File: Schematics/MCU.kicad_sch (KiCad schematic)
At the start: 28 parts, among them J1 Microsemi_FlashPro-JTAG-10, U1 STM32F405RGT6, Y1 8mhz

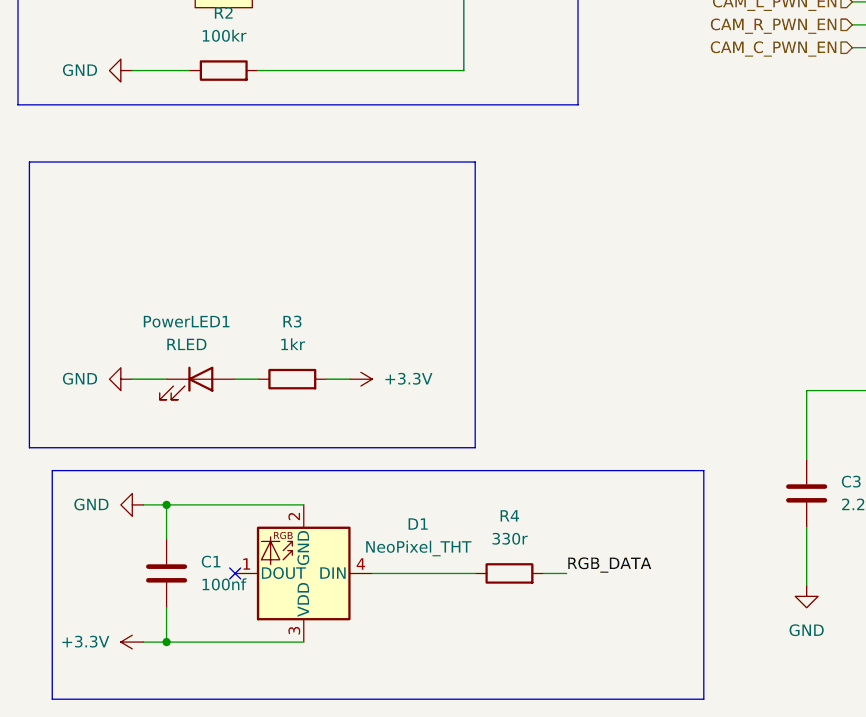
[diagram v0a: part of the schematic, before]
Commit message: dfm complete sent for order
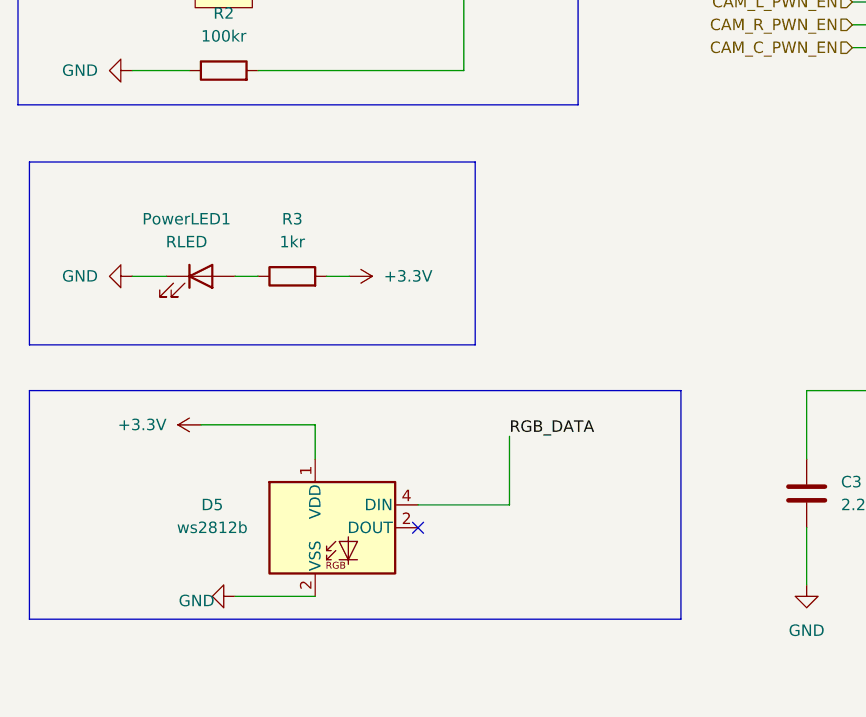
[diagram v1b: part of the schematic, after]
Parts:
- removed C1: 100nf, Capacitor_SMD:C_0805_2012Metric_Pad1.18x1.45mm_HandSolder, symbol Device:C
- removed D1: NeoPixel_THT, LED_SMD:LED_Kingbright_AAA3528ESGCT, symbol LED:NeoPixel_THT
- removed R4: 330r, Resistor_SMD:R_0805_2012Metric_Pad1.20x1.40mm_HandSolder, symbol Device:R
- added D5: ws2812b, LED_SMD:LED_WS2812B_PLCC4_5.0x5.0mm_P3.2mm, symbol LED:NeoPixel_THT
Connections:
- net +3.3V: now also D5.1 (VDD)
- net GND: now also D5.2 (DOUT)
- net RGB_DATA: now also D5.4 (DIN)
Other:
- moved on the sheet: PowerLED1, R3

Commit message: fixed can tranciver issues and updated to KiCad 10.0
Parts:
- J1: footprint myFootprints:CONN_7024610XX_MOL -> Connector_PinHeader_1.27mm:PinHeader_2x05_P1.27mm_Vertical

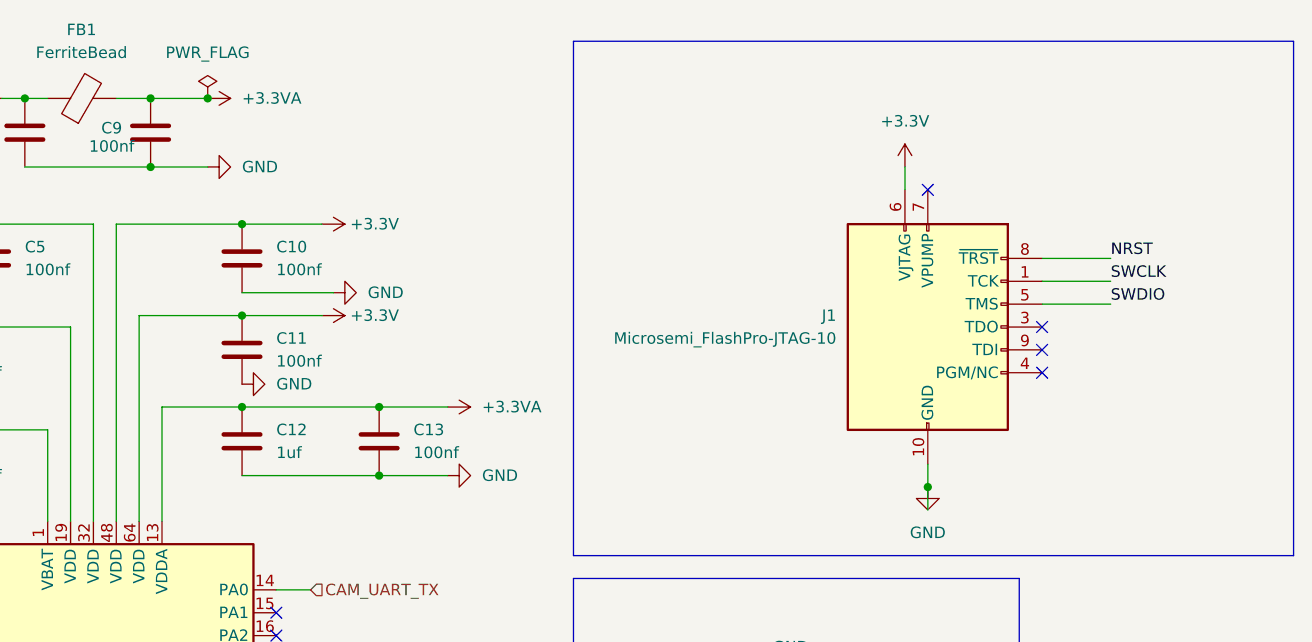
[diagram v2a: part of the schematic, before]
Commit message: updated stlink connector
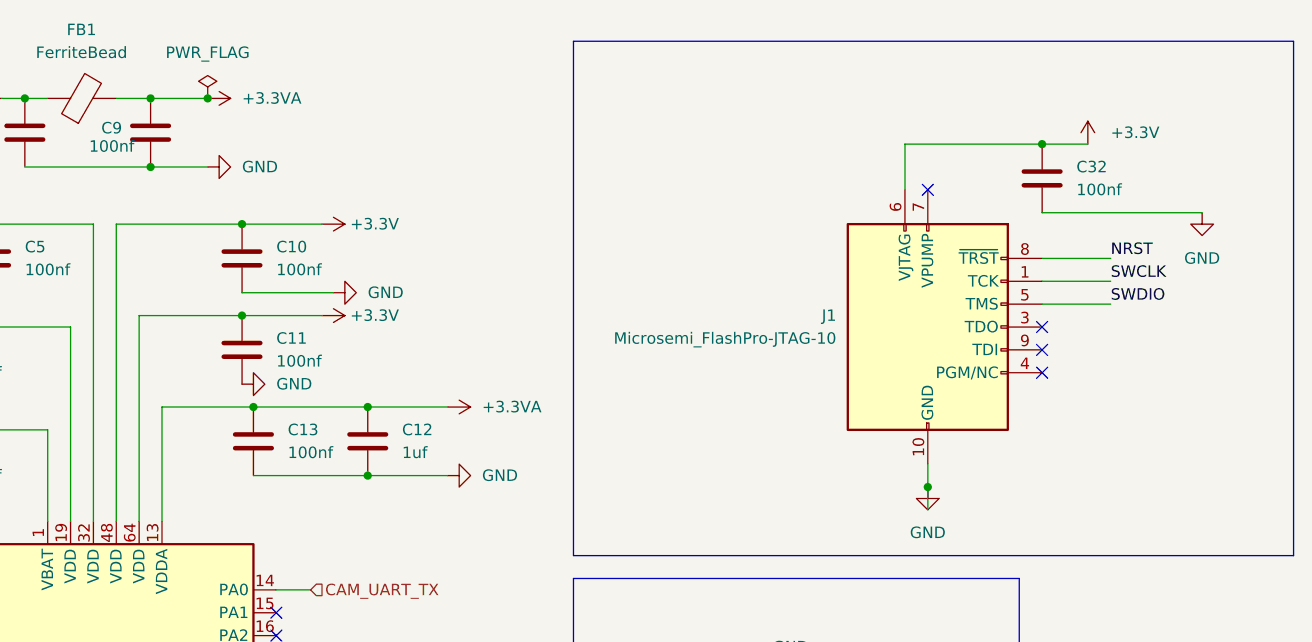
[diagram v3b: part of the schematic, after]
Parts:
- added C32: 100nf, Capacitor_SMD:C_0805_2012Metric_Pad1.18x1.45mm_HandSolder, symbol Device:C
- C14, C15: LCSC C53084486 -> C113825
- C3, C4: LCSC C19110 -> C377773
- C31: LCSC C98192 -> C1779
- J1: LCSC C588426 -> C22438120
- R2: LCSC C96346 -> C149504
- R3: LCSC C95781 -> C17513
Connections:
- net +3.3V: now also C32.1
- net GND: now also C32.2
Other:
- moved on the sheet: C12, C13
